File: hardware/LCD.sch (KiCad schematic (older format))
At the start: 32 parts, among them IC1 TPS61169DCKR, IC2 TPD4E001DRLR, IC3 AR1021-I/SS, U3 DS90CF364AMTD

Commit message: Routing board
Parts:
- removed C15, C16: 100n, Capacitor_SMD:C_0603_1608Metric, symbol antena:C
- added H1, H2, H3, H4: L_H, MountingHole:MountingHole_3.5mm_Pad_Via, symbol Mechanical:MountingHole_Pad
- R1, R2, R3, R4, R5: footprint EEZ DIB MCU r1B1:R0805 -> Resistor_SMD:R_0805_2012Metric
- R12: renamed from R?; footprint (none) -> Resistor_SMD:R_0805_2012Metric
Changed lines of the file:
@@
 F 0 "R2" V 3191 2050 59  0000 L BNN
 F 1 "10R" V 3280 2050 59  0000 L BNN
-F 2 "EEZ DIB MCU r1B1:R0805" H 3200 2000 50  0001 C CNN
+F 2 "Resistor_SMD:R_0805_2012Metric" H 3200 2000 50  0001 C CNN
 F 3 "" H 3200 2000 50  0001 C CNN
 	1    3200 2000
@@
 F 0 "R4" H 4175 5416 59  0000 R TNN
 F 1 "20K" H 4200 5170 59  0000 R BNN
-F 2 "EEZ DIB MCU r1B1:R0805" H 4100 5300 50  0001 C CNN
+F 2 "Resistor_SMD:R_0805_2012Metric" H 4100 5300 50  0001 C CNN
 F 3 "" H 4100 5300 50  0001 C CNN
 	1    4100 5300
@@
 F 0 "R3" H 3600 3540 59  0000 R TNN
 F 1 "10K" H 3600 3715 59  0000 R TNN
-F 2 "EEZ DIB MCU r1B1:R0805" H 3500 3600 50  0001 C CNN
+F 2 "Resistor_SMD:R_0805_2012Metric" H 3500 3600 50  0001 C CNN
 F 3 "" H 3500 3600 50  0001 C CNN
 	1    3500 3600
@@
 F 0 "R1" V 1791 1350 59  0000 R BNN
 F 1 "10R" V 1880 1350 59  0000 R BNN
-F 2 "EEZ DIB MCU r1B1:R0805" H 1800 1400 50  0001 C CNN
+F 2 "Resistor_SMD:R_0805_2012Metric" H 1800 1400 50  0001 C CNN
 F 3 "" H 1800 1400 50  0001 C CNN
 	1    1800 1400
@@
 F 0 "R5" H 5950 6341 59  0000 R TNN
 F 1 "4K7" H 5975 6530 59  0000 R TNN
-F 2 "EEZ DIB MCU r1B1:R0805" H 5900 6400 50  0001 C CNN
+F 2 "Resistor_SMD:R_0805_2012Metric" H 5900 6400 50  0001 C CNN
 F 3 "" H 5900 6400 50  0001 C CNN
 	1    5900 6400
@@
 Wire Wire Line
 	10100 6050 10100 6150
-Text GLabel 10500 5650 1    50   Input ~ 0
-3V3
-Text GLabel 10500 6150 3    50   Input ~ 0
-GND
-$Comp
-L antena:C C?
-U 1 1 5E384C86
-P 10500 5900
-AR Path="/5E22D431/5E384C86" Ref="C?"  Part="1"
-AR Path="/5E224865/5E384C86" Ref="C15"  Part="1"
-F 0 "C15" H 10615 5946 50  0000 L CNN
-F 1 "100n" H 10615 5855 50  0000 L CNN
-F 2 "Capacitor_SMD:C_0603_1608Metric" H 10538 5750 50  0001 C CNN
-F 3 "~" H 10500 5900 50  0001 C CNN
-	1    10500 5900
-	1    0    0    -1
-$EndComp
-Wire Wire Line
-	10500 5650 10500 5750
-Wire Wire Line
-	10500 6050 10500 6150
-Text GLabel 10900 5650 1    50   Input ~ 0
-3V3
-Text GLabel 10900 6150 3    50   Input ~ 0
-GND
-$Comp
-L antena:C C?
-U 1 1 5E384C91
-P 10900 5900
-AR Path="/5E22D431/5E384C91" Ref="C?"  Part="1"
-AR Path="/5E224865/5E384C91" Ref="C16"  Part="1"
-F 0 "C16" H 11015 5946 50  0000 L CNN
-F 1 "100n" H 11015 5855 50  0000 L CNN
-F 2 "Capacitor_SMD:C_0603_1608Metric" H 10938 5750 50  0001 C CNN
-F 3 "~" H 10900 5900 50  0001 C CNN
-	1    10900 5900
-	1    0    0    -1
-$EndComp
-Wire Wire Line
-	10900 5650 10900 5750
-Wire Wire Line
-	10900 6050 10900 6150
 Text GLabel 8050 5650 1    50   Input ~ 0
 3V3
@@
 $EndComp
 $Comp
-L antena:R R?
+L antena:R R12
 U 1 1 5E356688
 P 7750 3350
-F 0 "R?" V 7543 3350 50  0000 C CNN
+F 0 "R12" V 7543 3350 50  0000 C CNN
 F 1 "10K" V 7634 3350 50  0000 C CNN
-F 2 "" V 7680 3350 50  0001 C CNN
+F 2 "Resistor_SMD:R_0805_2012Metric" V 7680 3350 50  0001 C CNN
 F 3 "~" H 7750 3350 50  0001 C CNN
 	1    7750 3350
@@
 Wire Wire Line
 	7450 3350 7600 3350
+$Comp
+L Mechanical:MountingHole_Pad H1
+U 1 1 5E40C78F
+P 950 3050
+F 0 "H1" H 1050 3101 50  0000 L CNN
+F 1 "L_H" H 1050 3010 50  0000 L CNN
+F 2 "MountingHole:MountingHole_3.5mm_Pad_Via" H 950 3050 50  0001 C CNN
+F 3 "~" H 950 3050 50  0001 C CNN
+	1    950  3050
+	1    0    0    -1
+$EndComp
+$Comp
+L Mechanical:MountingHole_Pad H4
+U 1 1 5E40C803
+P 1250 3350
+F 0 "H4" H 1350 3401 50  0000 L CNN
+F 1 "L_H" H 1350 3310 50  0000 L CNN
+F 2 "MountingHole:MountingHole_3.5mm_Pad_Via" H 1250 3350 50  0001 C CNN
+F 3 "~" H 1250 3350 50  0001 C CNN
+	1    1250 3350
+	1    0    0    -1
+$EndComp
+$Comp
+L Mechanical:MountingHole_Pad H3
+U 1 1 5E40C855
+P 1250 3050
+F 0 "H3" H 1350 3101 50  0000 L CNN
+F 1 "L_H" H 1350 3010 50  0000 L CNN
+F 2 "MountingHole:MountingHole_3.5mm_Pad_Via" H 1250 3050 50  0001 C CNN
+F 3 "~" H 1250 3050 50  0001 C CNN
+	1    1250 3050
+	1    0    0    -1
+$EndComp
+$Comp
+L Mechanical:MountingHole_Pad H2
+U 1 1 5E40C8A9
+P 950 3350
+F 0 "H2" H 1050 3401 50  0000 L CNN
+F 1 "L_H" H 1050 3310 50  0000 L CNN
+F 2 "MountingHole:MountingHole_3.5mm_Pad_Via" H 950 3350 50  0001 C CNN
+F 3 "~" H 950 3350 50  0001 C CNN
+	1    950  3350
+	1    0    0    -1
+$EndComp
+$Comp
+L LCD_PMOD-rescue:GND-EEZ_DIB_MCU_r1B2-eagle-import #SUPPLY?
+U 1 0 5E3E2395
+P 1100 4400
+AR Path="/5E3E2395" Ref="#SUPPLY?"  Part="1"
+AR Path="/5B8E2134/5E3E2395" Ref="#SUPPLY?"  Part="1"
+AR Path="/5E224865/5E3E2395" Ref="#SUPPLY0112"  Part="1"
+F 0 "#SUPPLY0112" H 1100 4400 50  0001 C CNN
+F 1 "GND" H 1000 4250 59  0000 L BNN
+F 2 "" H 1100 4400 50  0001 C CNN
+F 3 "" H 1100 4400 50  0001 C CNN
+	1    1100 4400
+	1    0    0    -1
+$EndComp
+Text GLabel 1000 4100 1    50   Input ~ 0
+AGND
+Wire Wire Line
+	1000 4100 1000 4200
+Wire Wire Line
+	1000 4200 1100 4200
+Wire Wire Line
+	1100 4200 1100 4300
+Text GLabel 1200 4100 1    50   Input ~ 0
+ADC_REFGND
+Wire Wire Line
+	1200 4100 1200 4200
+Wire Wire Line
+	1200 4200 1100 4200
 Wire Bus Line
 	6175 2700 6175 3200
@@
 Wire Bus Line
 	6175 1900 6175 2400
+Connection ~ 1100 4200
 $EndSCHEMATC

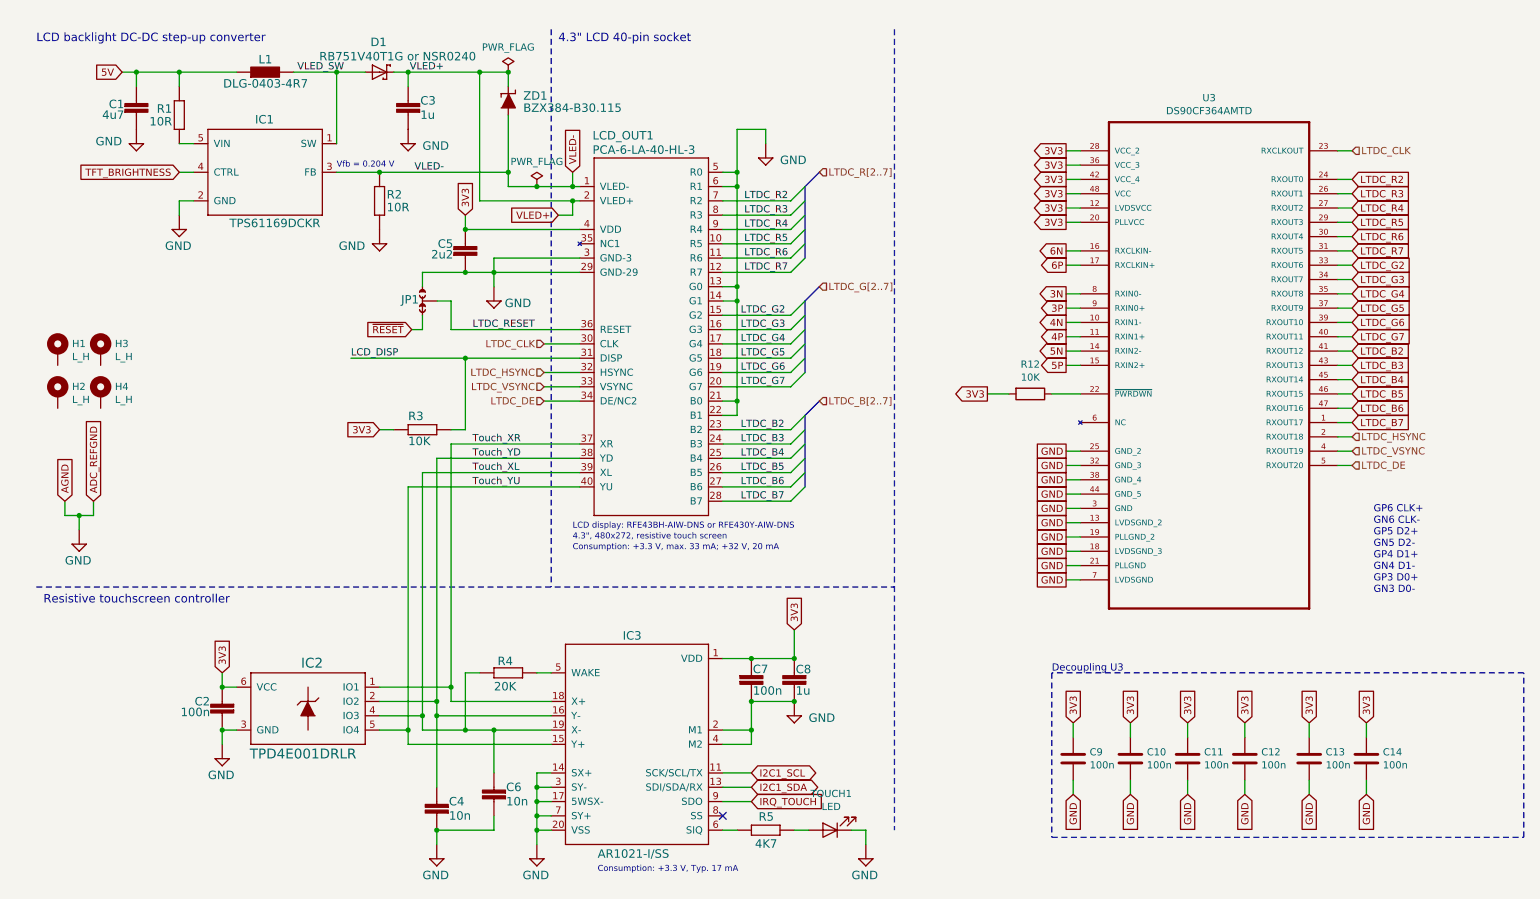
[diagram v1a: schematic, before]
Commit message: Before AGND - GND
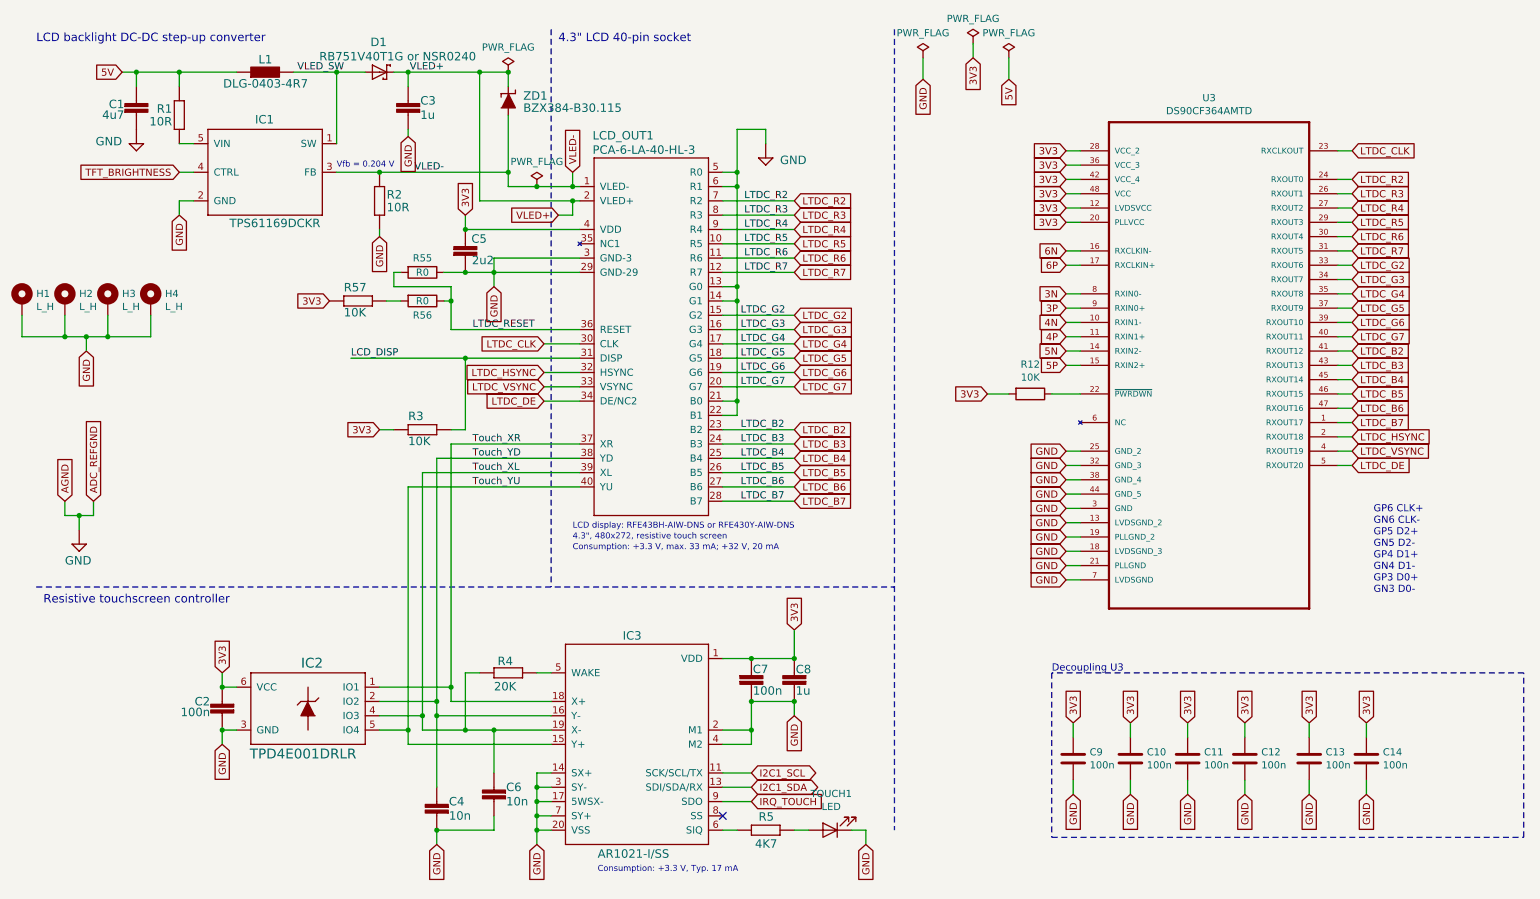
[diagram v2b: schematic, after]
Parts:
- removed JP1: JP3-CUT, EEZ DIB MCU r1B1:JP3-CUT, symbol LCD_PMOD-rescue:JP3-CUT-EEZ_DIB_MCU_r1B2-eagle-import
- added R55, R56: R0, Resistor_SMD:R_0201_0603Metric, symbol antena:R
- added R57: 10K, Resistor_SMD:R_0805_2012Metric, symbol LCD_PMOD-rescue:R-EU_R0805-EEZ_DIB_MCU_r1B2-eagle-import
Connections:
- net 3V3: now also R57.2
- net GND: now also C2.1, C3.2, C4.2, C5.2, C6.2, C7.1, C8.1, H1.1, H2.1, H3.1, H4.1, IC1.2 (GND), IC2.3 (GND), IC3.14 (SX+), IC3.17 (5WSX-), IC3.2 (M1), IC3.20 (VSS), IC3.3 (SY-), IC3.4 (M2), IC3.7 (SY+), LCD_OUT1.29 (GND-29), LCD_OUT1.3 (GND-3), R2.2, TOUCH1.1 (K), R55.1
- net LTDC_RESET: now also R55.2, R56.1
- new net: R56.2, R57.1
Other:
- moved on the sheet: H1, H2, H3, H4

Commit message: Finishing routing
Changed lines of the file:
@@
 	1    0    0    -1
 $EndComp
-$Comp
-L LCD_PMOD-rescue:GND-EEZ_DIB_MCU_r1B2-eagle-import #SUPPLY?
-U 1 0 5E3E2395
-P 1100 4400
-AR Path="/5E3E2395" Ref="#SUPPLY?"  Part="1"
-AR Path="/5B8E2134/5E3E2395" Ref="#SUPPLY?"  Part="1"
-AR Path="/5E224865/5E3E2395" Ref="#SUPPLY0112"  Part="1"
-F 0 "#SUPPLY0112" H 1100 4400 50  0001 C CNN
-F 1 "GND" H 1000 4250 59  0000 L BNN
-F 2 "" H 1100 4400 50  0001 C CNN
-F 3 "" H 1100 4400 50  0001 C CNN
-	1    1100 4400
-	1    0    0    -1
-$EndComp
-Text GLabel 1000 4100 1    50   Input ~ 0
-AGND
-Wire Wire Line
-	1000 4100 1000 4200
-Wire Wire Line
-	1000 4200 1100 4200
-Wire Wire Line
-	1100 4200 1100 4300
-Text GLabel 1200 4100 1    50   Input ~ 0
-ADC_REFGND
-Wire Wire Line
-	1200 4100 1200 4200
-Wire Wire Line
-	1200 4200 1100 4200
-Connection ~ 1100 4200
 Text GLabel 10000 1650 2    50   Input ~ 0
 LTDC_CLK
